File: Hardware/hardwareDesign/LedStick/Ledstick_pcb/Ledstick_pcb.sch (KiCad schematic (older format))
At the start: 39 parts

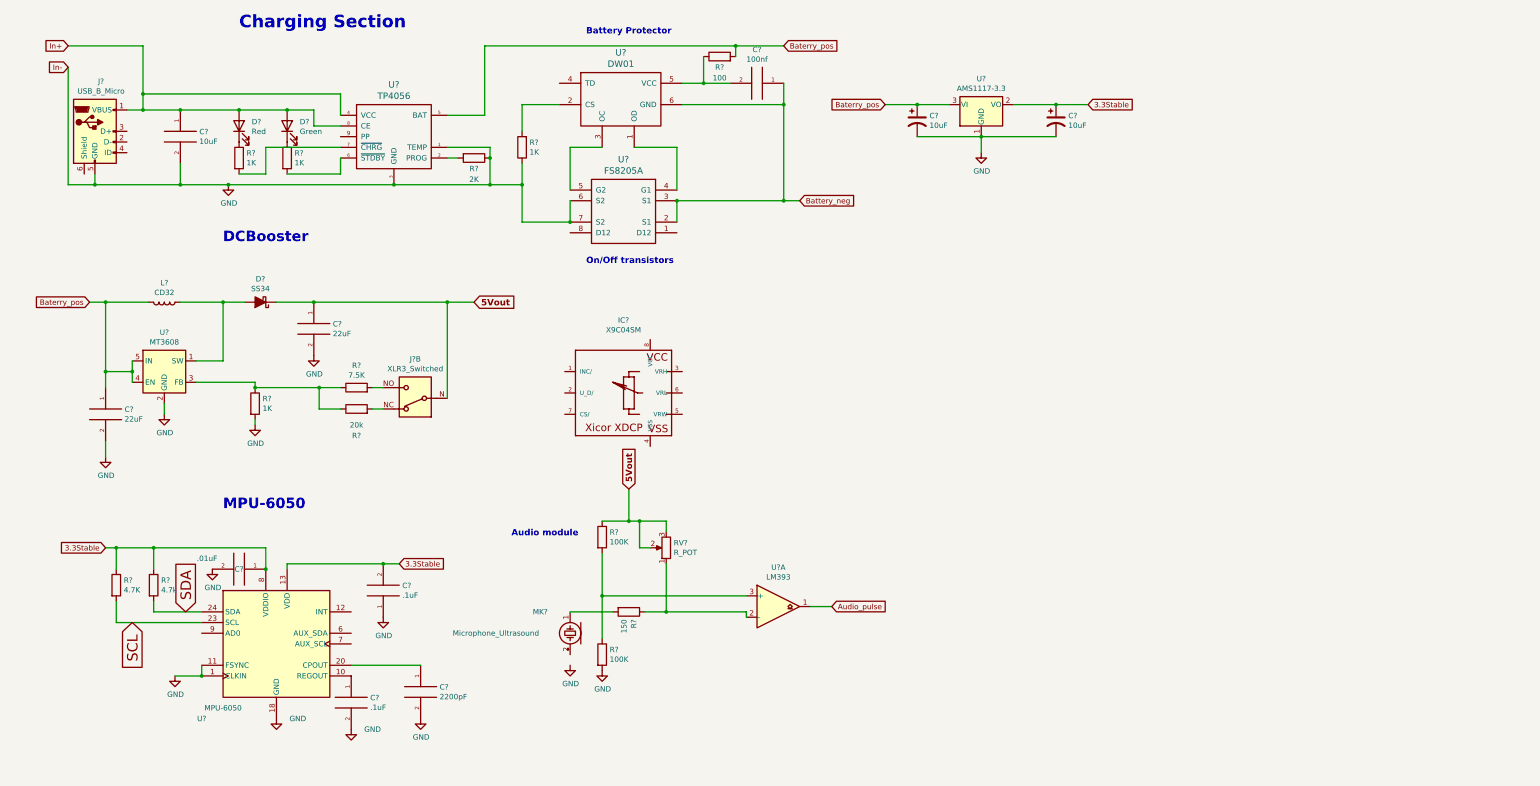
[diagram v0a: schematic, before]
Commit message: Adding leds and schematic almost done, audio pending
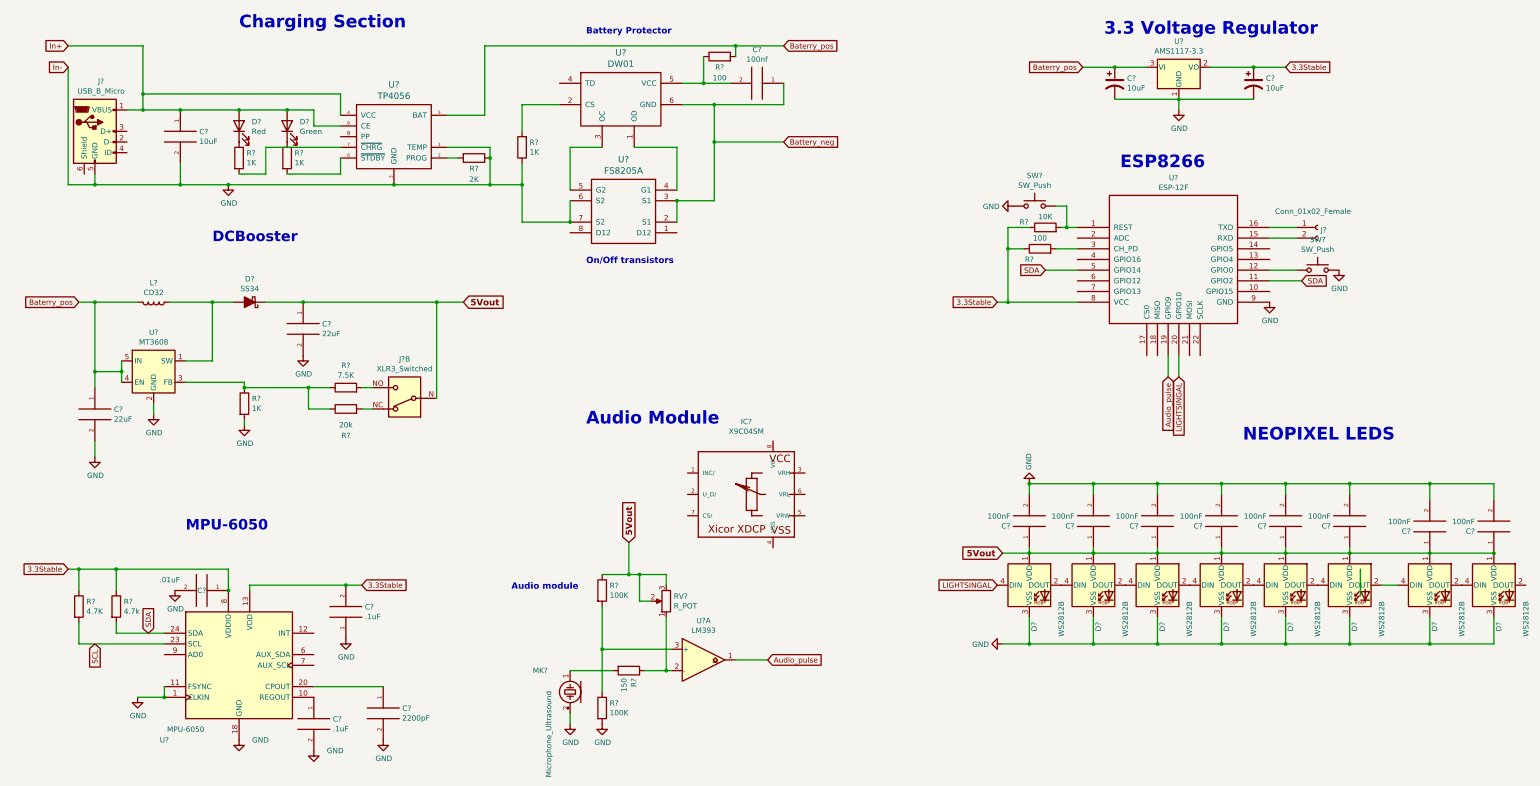
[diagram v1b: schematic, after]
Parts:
- added C? (x8): 100nF, symbol pspice:CAP
- added D? (x8): WS2812B, LED_SMD:LED_WS2812B_PLCC4_5.0x5.0mm_P3.2mm, symbol LED:WS2812B
- added J?: Conn_01x02_Female, symbol Connector:Conn_01x02_Female
- added R?: 100, symbol Device:R
- added R?: 10K, symbol Device:R
- added SW? (x2): SW_Push, symbol Switch:SW_Push
- added U?: ESP-12F, symbol ESP8266:ESP-12F
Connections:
- net 3.3Stable: now also R?.1, R?.1, U?.8 (VCC)
- net 5Vout: now also C?.1, C?.1, C?.1, C?.1, C?.1, C?.1, C?.1, C?.1, D?.1 (VDD), D?.1 (VDD), D?.1 (VDD), D?.1 (VDD), D?.1 (VDD), D?.1 (VDD), D?.1 (VDD), D?.1 (VDD)
- net Audio_pulse: now also U?.19 (GPIO9)
- net GND: now also MK?.2 (+), C?.2, C?.2, C?.2, C?.2, C?.2, C?.2, C?.2, C?.2, D?.3 (VSS), D?.3 (VSS), D?.3 (VSS), D?.3 (VSS), D?.3 (VSS), D?.3 (VSS), D?.3 (VSS), D?.3 (VSS), SW?.1, SW?.2, U?.9 (GND)
- net SDA: now also U?.11 (GPIO2), U?.5 (GPIO14)
- new net: R?.2, SW?.2, U?.1 (REST)
- new net: SW?.1, U?.12 (GPIO0)
- new net: J?.2 (Pin_2), U?.15 (RXD)
- new net: J?.1 (Pin_1), U?.16 (TXD)
- new net: R?.2, U?.3 (CH_PD)
- new net: D?.2 (DOUT), D?.4 (DIN) (x7)
- new net LIGHTSINGAL: D?.4 (DIN), U?.20 (GPIO10)
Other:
- note added: "3.3 Voltage Regulator\n\n"
- note added: "Audio Module\n\n"
- note added: "ESP8266\n\n"
- note added: "NEOPIXEL LEDS\n\n"
- moved on the sheet: C?, D?, IC?, J?B, L?, MK?, R?, RV?, U?, U?A
